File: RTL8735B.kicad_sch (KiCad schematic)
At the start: 26 parts, among them SW1 EVQ-PUB02K, SW2 EVQ-PUB02K, U1 W25Q128JVSIQ, U2 RTL8735BDM-A20-N04

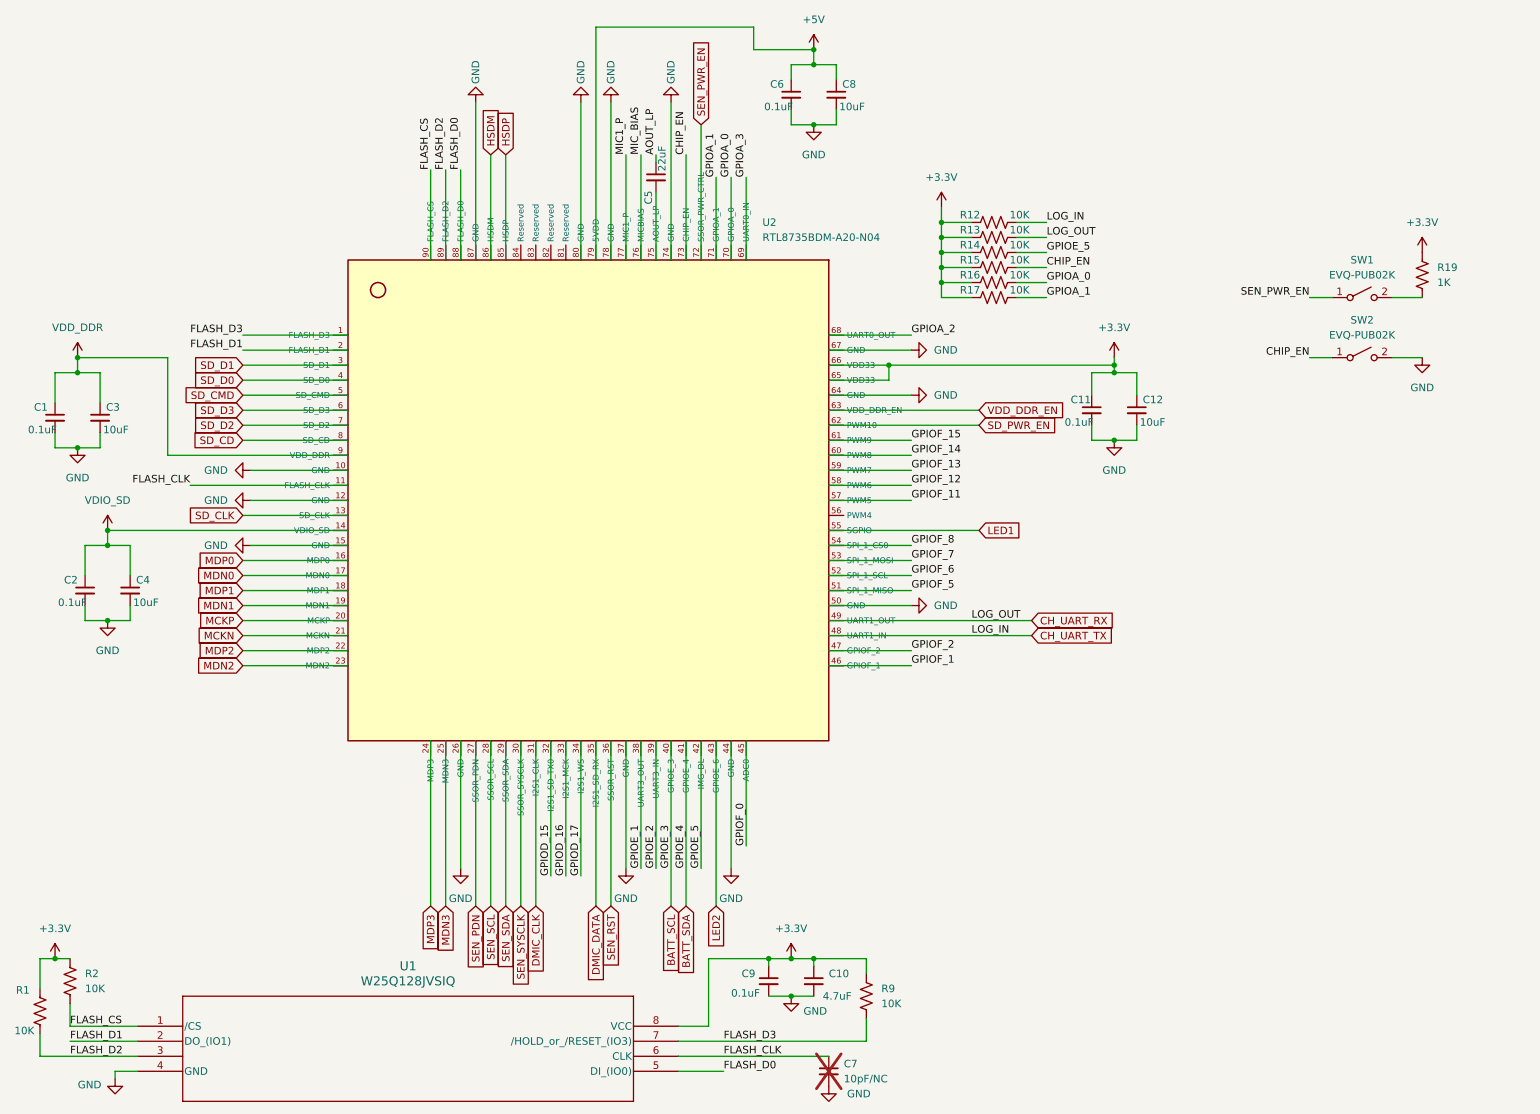
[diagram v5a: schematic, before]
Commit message: Replaced all passive footprints from 0603 metric to 0603 imperial. Big oversight. All done. Next is DRC
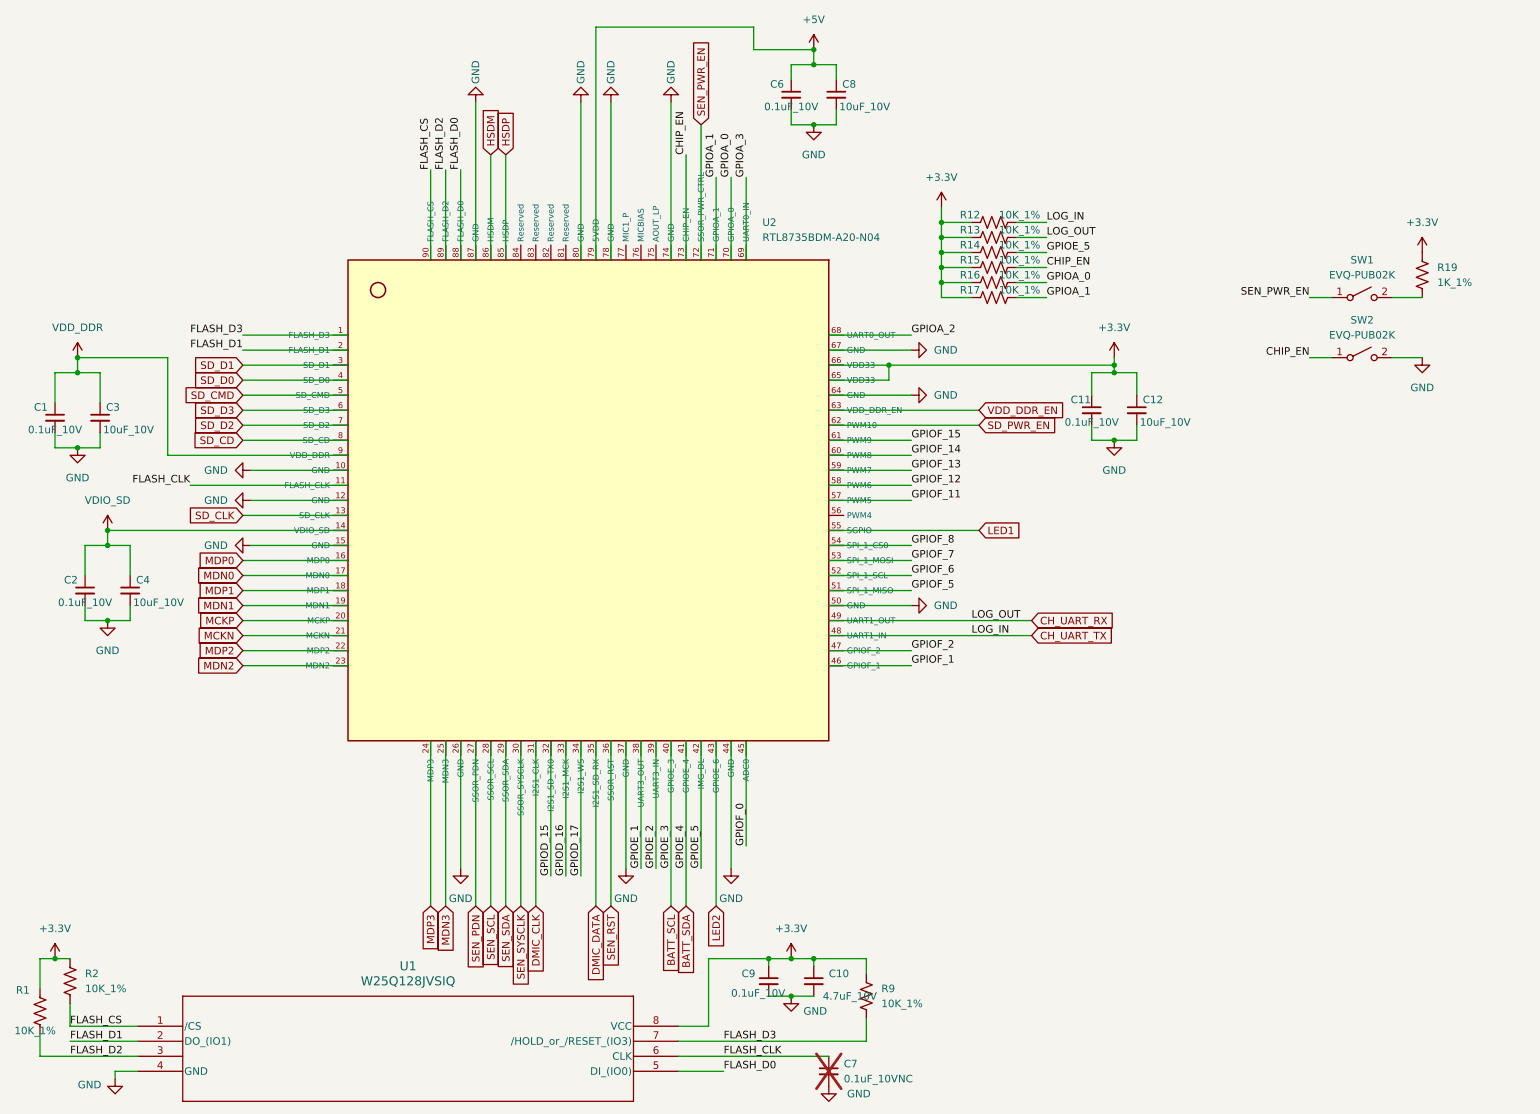
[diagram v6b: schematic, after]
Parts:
- removed C5: 22uF, Capacitor_SMD:C_0201_0603Metric_Pad0.64x0.40mm_HandSolder, symbol Device:C_Small
- C1, C11, C2, C6, C9: value 0.1uF -> 0.1uF_10V; footprint Capacitor_SMD:C_0201_0603Metric_Pad0.64x0.40mm_HandSolder -> Capacitor_SMD:C_0603_1608Metric
- C10: value 4.7uF -> 4.7uF_10V; footprint Capacitor_SMD:C_0201_0603Metric_Pad0.64x0.40mm_HandSolder -> Capacitor_SMD:C_0603_1608Metric
- C12, C3, C4, C8: value 10uF -> 10uF_10V; footprint Capacitor_SMD:C_0201_0603Metric_Pad0.64x0.40mm_HandSolder -> Capacitor_SMD:C_0603_1608Metric
- C7: value 10pF/NC -> 0.1uF_10VNC; footprint Capacitor_SMD:C_0201_0603Metric_Pad0.64x0.40mm_HandSolder -> Capacitor_SMD:C_0603_1608Metric
- R1, R12, R13, R14, R15, R16, R17, R2, R9: value 10K -> 10K_1%; footprint Resistor_SMD:R_0201_0603Metric_Pad0.64x0.40mm_HandSolder -> Resistor_SMD:R_0603_1608Metric
- R19: value 1K -> 1K_1%; footprint Resistor_SMD:R_0201_0603Metric_Pad0.64x0.40mm_HandSolder -> Resistor_SMD:R_0603_1608Metric
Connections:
- net MIC1_P: no longer names the net of U2.77 (MIC1_P)
- net MIC_BIAS: no longer names the net of U2.76 (MICBIAS)
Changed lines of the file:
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@@
 	(wire
 		(pts
-			(xy 118.11 36.83) (xy 118.11 54.61)
-		)
-		(stroke
-			(width 0)
-			(type default)
-		)
-	)
-	(wire
-		(pts
 			(xy 198.12 72.39) (xy 198.12 71.12)
 		)
@@
 	(wire
 		(pts
-			(xy 115.57 36.83) (xy 115.57 54.61)
-		)
-		(stroke
-			(width 0)
-			(type default)
-		)
-	)
-	(wire
-		(pts
 			(xy 151.13 31.75) (xy 147.32 31.75)
 		)
@@
 	(wire
 		(pts
-			(xy 120.65 36.83) (xy 120.65 38.1)
-		)
-		(stroke
-			(width 0)
-			(type default)
-		)
-	)
-	(wire
-		(pts
 			(xy 181.61 53.34) (xy 186.69 53.34)
 		)
@@
 	(wire
 		(pts
-			(xy 120.65 43.18) (xy 120.65 54.61)
-		)
-		(stroke
-			(width 0)
-			(type default)
-		)
-	)
-	(wire
-		(pts
 			(xy 181.61 58.42) (xy 186.69 58.42)
 		)
@@
 		)
 	)
-	(label "MIC_BIAS"
-		(at 118.11 36.83 90)
-		(effects
-			(font
-				(size 1.27 1.27)
-			)
-			(justify left bottom)
-		)
-	)
 	(label "GPIOA_2"
 		(at 163.83 67.31 0)
@@
 		)
 	)
-	(label "AOUT_LP"
-		(at 120.65 36.83 90)
-		(effects
-			(font
-				(size 1.27 1.27)
-			)
-			(justify left bottom)
-		)
-	)
 	(label "GPIOE_3"
 		(at 123.19 157.48 90)
@@
 		)
 	)
-	(label "MIC1_P"
-		(at 115.57 36.83 90)
-		(effects
-			(font
-				(size 1.27 1.27)
-			)
-			(justify left bottom)
-		)
-	)
 	(label "FLASH_D1"
 		(at 50.8 69.85 180)
@@
 			)
 		)
-		(property "Value" "10K"
+		(property "Value" "10K_1%"
 			(at 182.118 57.15 90)
 			(effects
@@
 			)
 		)
-		(property "Footprint" "Resistor_SMD:R_0201_0603Metric_Pad0.64x0.40mm_HandSolder"
+		(property "Footprint" "Resistor_SMD:R_0603_1608Metric"
 			(at 178.054 57.404 90)
 			(effects
@@
 			)
 		)
-		(property "Value" "10K"
+		(property "Value" "10K_1%"
 			(at 182.118 46.99 90)
 			(effects
@@
 			)
 		)
-		(property "Footprint" "Resistor_SMD:R_0201_0603Metric_Pad0.64x0.40mm_HandSolder"
+		(property "Footprint" "Resistor_SMD:R_0603_1608Metric"
 			(at 178.054 47.244 90)
 			(effects
@@
 			)
 		)
-		(property "Value" "10K"
+		(property "Value" "10K_1%"
 			(at 182.118 52.07 90)
 			(effects
@@
 			)
 		)
-		(property "Footprint" "Resistor_SMD:R_0201_0603Metric_Pad0.64x0.40mm_HandSolder"
+		(property "Footprint" "Resistor_SMD:R_0603_1608Metric"
 			(at 178.054 52.324 90)
 			(effects
@@
 			)
 		)
-		(property "Value" "10K"
+		(property "Value" "10K_1%"
 			(at 182.118 49.53 90)
 			(effects
@@
 			)
 		)
-		(property "Footprint" "Resistor_SMD:R_0201_0603Metric_Pad0.64x0.40mm_HandSolder"
+		(property "Footprint" "Resistor_SMD:R_0603_1608Metric"
 			(at 178.054 49.784 90)
 			(effects
@@
 			)
 		)
-		(property "Value" "4.7uF"
+		(property "Value" "4.7uF_10V"
 			(at 148.844 179.07 0)
 			(effects
@@
 			)
 		)
-		(property "Footprint" "Capacitor_SMD:C_0201_0603Metric_Pad0.64x0.40mm_HandSolder"
+		(property "Footprint" "Capacitor_SMD:C_0603_1608Metric"
 			(at 147.32 176.53 0)
 			(effects
@@
 			)
 		)
-		(property "Value" "0.1uF"
+		(property "Value" "0.1uF_10V"
 			(at 19.558 112.522 0)
 			(effects
@@
 			)
 		)
-		(property "Footprint" "Capacitor_SMD:C_0201_0603Metric_Pad0.64x0.40mm_HandSolder"
+		(property "Footprint" "Capacitor_SMD:C_0603_1608Metric"
 			(at 24.13 110.49 0)
 			(effects
@@
 			)
 		)
-		(property "Value" "10K"
+		(property "Value" "10K_1%"
 			(at 182.118 59.69 90)
 			(effects
@@
 			)
 		)
-		(property "Footprint" "Resistor_SMD:R_0201_0603Metric_Pad0.64x0.40mm_HandSolder"
+		(property "Footprint" "Resistor_SMD:R_0603_1608Metric"
 			(at 178.054 59.944 90)
 			(effects
@@
 			)
 		)
-		(property "Value" "10K"
+		(property "Value" "10K_1%"
 			(at 158.75 180.3399 0)
 			(effects
@@
 			)
 		)
-		(property "Footprint" "Resistor_SMD:R_0201_0603Metric_Pad0.64x0.40mm_HandSolder"
+		(property "Footprint" "Resistor_SMD:R_0603_1608Metric"
 			(at 157.226 179.324 90)
 			(effects
@@
 			)
 		)
-		(property "Value" "0.1uF"
+		(property "Value" "0.1uF_10V"
 			(at 133.35 178.562 0)
 			(effects
@@
 			)
 		)
-		(property "Footprint" "Capacitor_SMD:C_0201_0603Metric_Pad0.64x0.40mm_HandSolder"
+		(property "Footprint" "Capacitor_SMD:C_0603_1608Metric"
 			(at 139.7 176.53 0)
 			(effects
@@
 			)
 		)
-		(property "Value" "10uF"
+		(property "Value" "10uF_10V"
 			(at 32.258 112.522 0)
 			(effects
@@
 			)
 		)
-		(property "Footprint" "Capacitor_SMD:C_0201_0603Metric_Pad0.64x0.40mm_HandSolder"
+		(property "Footprint" "Capacitor_SMD:C_0603_1608Metric"
 			(at 31.75 110.49 0)
 			(effects
@@
 			)
 		)
-		(property "Value" "0.1uF"
+		(property "Value" "0.1uF_10V"
 			(at 189.738 82.042 0)
 			(effects
@@
 			)
 		)
-		(property "Footprint" "Capacitor_SMD:C_0201_0603Metric_Pad0.64x0.40mm_HandSolder"
+		(property "Footprint" "Capacitor_SMD:C_0603_1608Metric"
 			(at 194.31 80.01 0)
 			(effects
@@
 			)
 		)
-		(property "Value" "10K"
+		(property "Value" "10K_1%"
 			(at 182.118 54.61 90)
 			(effects
@@
 			)
 		)
-		(property "Footprint" "Resistor_SMD:R_0201_0603Metric_Pad0.64x0.40mm_HandSolder"
+		(property "Footprint" "Resistor_SMD:R_0603_1608Metric"
 			(at 178.054 54.864 90)
 			(effects
@@
 			)
 		)
-		(property "Value" "10K"
+		(property "Value" "10K_1%"
 			(at 12.192 184.912 0)
 			(effects
@@
 			)
 		)
-		(property "Footprint" "Resistor_SMD:R_0201_0603Metric_Pad0.64x0.40mm_HandSolder"
+		(property "Footprint" "Resistor_SMD:R_0603_1608Metric"
 			(at 17.526 181.864 90)
 			(effects
@@
 			)
 		)
-		(property "Value" "10uF"
+		(property "Value" "10uF_10V"
 			(at 202.438 82.042 0)
 			(effects
@@
 			)
 		)
-		(property "Footprint" "Capacitor_SMD:C_0201_0603Metric_Pad0.64x0.40mm_HandSolder"
+		(property "Footprint" "Capacitor_SMD:C_0603_1608Metric"
 			(at 201.93 80.01 0)
 			(effects
@@
 			)
 		)
-		(property "Value" "10uF"
+		(property "Value" "10uF_10V"
 			(at 151.638 28.702 0)
 			(effects
@@
 			)
 		)
-		(property "Footprint" "Capacitor_SMD:C_0201_0603Metric_Pad0.64x0.40mm_HandSolder"
+		(property "Footprint" "Capacitor_SMD:C_0603_1608Metric"
 			(at 151.13 26.67 0)
 			(effects
@@
 	)
 	(symbol
-		(lib_id "Device:C_Small")
-		(at 120.65 40.64 0)
-		(unit 1)
-		(exclude_from_sim no)
-		(in_bom yes)
-		(on_board yes)
-		(dnp no)
-		(property "Reference" "C5"
-			(at 119.38 45.212 90)
-			(effects
-				(font
-					(size 1.27 1.27)
-				)
-				(justify left)
-			)
-		)
-		(property "Value" "22uF"
-			(at 121.666 39.624 90)
-			(effects
-				(font
-					(size 1.27 1.27)
-				)
-				(justify left)
-			)
-		)
-		(property "Footprint" "Capacitor_SMD:C_0201_0603Metric_Pad0.64x0.40mm_HandSolder"
-			(at 120.65 40.64 0)
-			(effects
-				(font
-					(size 1.27 1.27)
-				)
-				(hide yes)
-			)
-		)
-		(property "Datasheet" "~"
-			(at 120.65 40.64 0)
-			(effects
-				(font
-					(size 1.27 1.27)
-				)
-				(hide yes)
-			)
-		)
-		(property "Description" "Unpolarized capacitor, small symbol"
-			(at 120.65 40.64 0)
-			(effects
-				(font
-					(size 1.27 1.27)
-				)
-				(hide yes)
-			)
-		)
-		(pin "2"
-		)
-		(pin "1"
-		)
-		(instances
-			(project "mormee-board-1"
-				(path "/d2af8ba6-fbfa-439f-91d9-67827f3f2396/2ed075f5-8bb4-40ff-9b8c-12d3a7838d36"
-					(reference "C5")
-					(unit 1)
-				)
-			)
-		)
-	)
-	(symbol
 		(lib_id "power:+3.3V")
 		(at 147.32 19.05 0)
@@
 			)
 		)
-		(property "Value" "10K"
+		(property "Value" "10K_1%"
 			(at 24.13 177.7999 0)
 			(effects
@@
 			)
 		)
-		(property "Footprint" "Resistor_SMD:R_0201_0603Metric_Pad0.64x0.40mm_HandSolder"
+		(property "Footprint" "Resistor_SMD:R_0603_1608Metric"
 			(at 22.606 176.784 90)
 			(effects
@@
 			)
 		)
-		(property "Value" "0.1uF"
+		(property "Value" "0.1uF_10V"
 			(at 138.938 28.702 0)
 			(effects
@@
 			)
 		)
-		(property "Footprint" "Capacitor_SMD:C_0201_0603Metric_Pad0.64x0.40mm_HandSolder"
+		(property "Footprint" "Capacitor_SMD:C_0603_1608Metric"
 			(at 143.51 26.67 0)
 			(effects
@@
 			)
 		)
-		(property "Value" "1K"
+		(property "Value" "1K_1%"
 			(at 252.73 58.4199 0)
 			(effects
@@
 			)
 		)
-		(property "Footprint" "Resistor_SMD:R_0201_0603Metric_Pad0.64x0.40mm_HandSolder"
+		(property "Footprint" "Resistor_SMD:R_0603_1608Metric"
 			(at 251.206 57.404 90)
 			(effects
@@
 			)
 		)
-		(property "Value" "10pF/NC"
+		(property "Value" "0.1uF_10VNC"
 			(at 152.4 193.0462 0)
 			(effects
@@
 			)
 		)
-		(property "Footprint" "Capacitor_SMD:C_0201_0603Metric_Pad0.64x0.40mm_HandSolder"
+		(property "Footprint" "Capacitor_SMD:C_0603_1608Metric"
 			(at 149.86 191.77 0)
 			(effects
@@
 			)
 		)
-		(property "Value" "0.1uF"
+		(property "Value" "0.1uF_10V"
 			(at 14.478 83.312 0)
 			(effects
@@
 			)
 		)
-		(property "Footprint" "Capacitor_SMD:C_0201_0603Metric_Pad0.64x0.40mm_HandSolder"
+		(property "Footprint" "Capacitor_SMD:C_0603_1608Metric"
 			(at 19.05 81.28 0)
 			(effects
@@
 			)
 		)
-		(property "Value" "10uF"
+		(property "Value" "10uF_10V"
 			(at 27.178 83.312 0)
 			(effects
@@
 			)
 		)
-		(property "Footprint" "Capacitor_SMD:C_0201_0603Metric_Pad0.64x0.40mm_HandSolder"
+		(property "Footprint" "Capacitor_SMD:C_0603_1608Metric"
 			(at 26.67 81.28 0)
 			(effects

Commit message: All fiducials and mounting holes placed. Except one hole, which I'll try to place. WIP
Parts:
- U1: footprint SOIC_128JVSIQ_WIN -> W25Q128JVSIQ:SOIC_128JVSIQ_WIN
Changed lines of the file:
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@@
 			)
 		)
-		(property "Footprint" "SOIC_128JVSIQ_WIN"
+		(property "Footprint" "W25Q128JVSIQ:SOIC_128JVSIQ_WIN"
 			(at 33.02 184.15 0)
 			(effects
